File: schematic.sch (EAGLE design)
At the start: 65 parts, among them U1 ADP3338AKCZ-3.3RL7

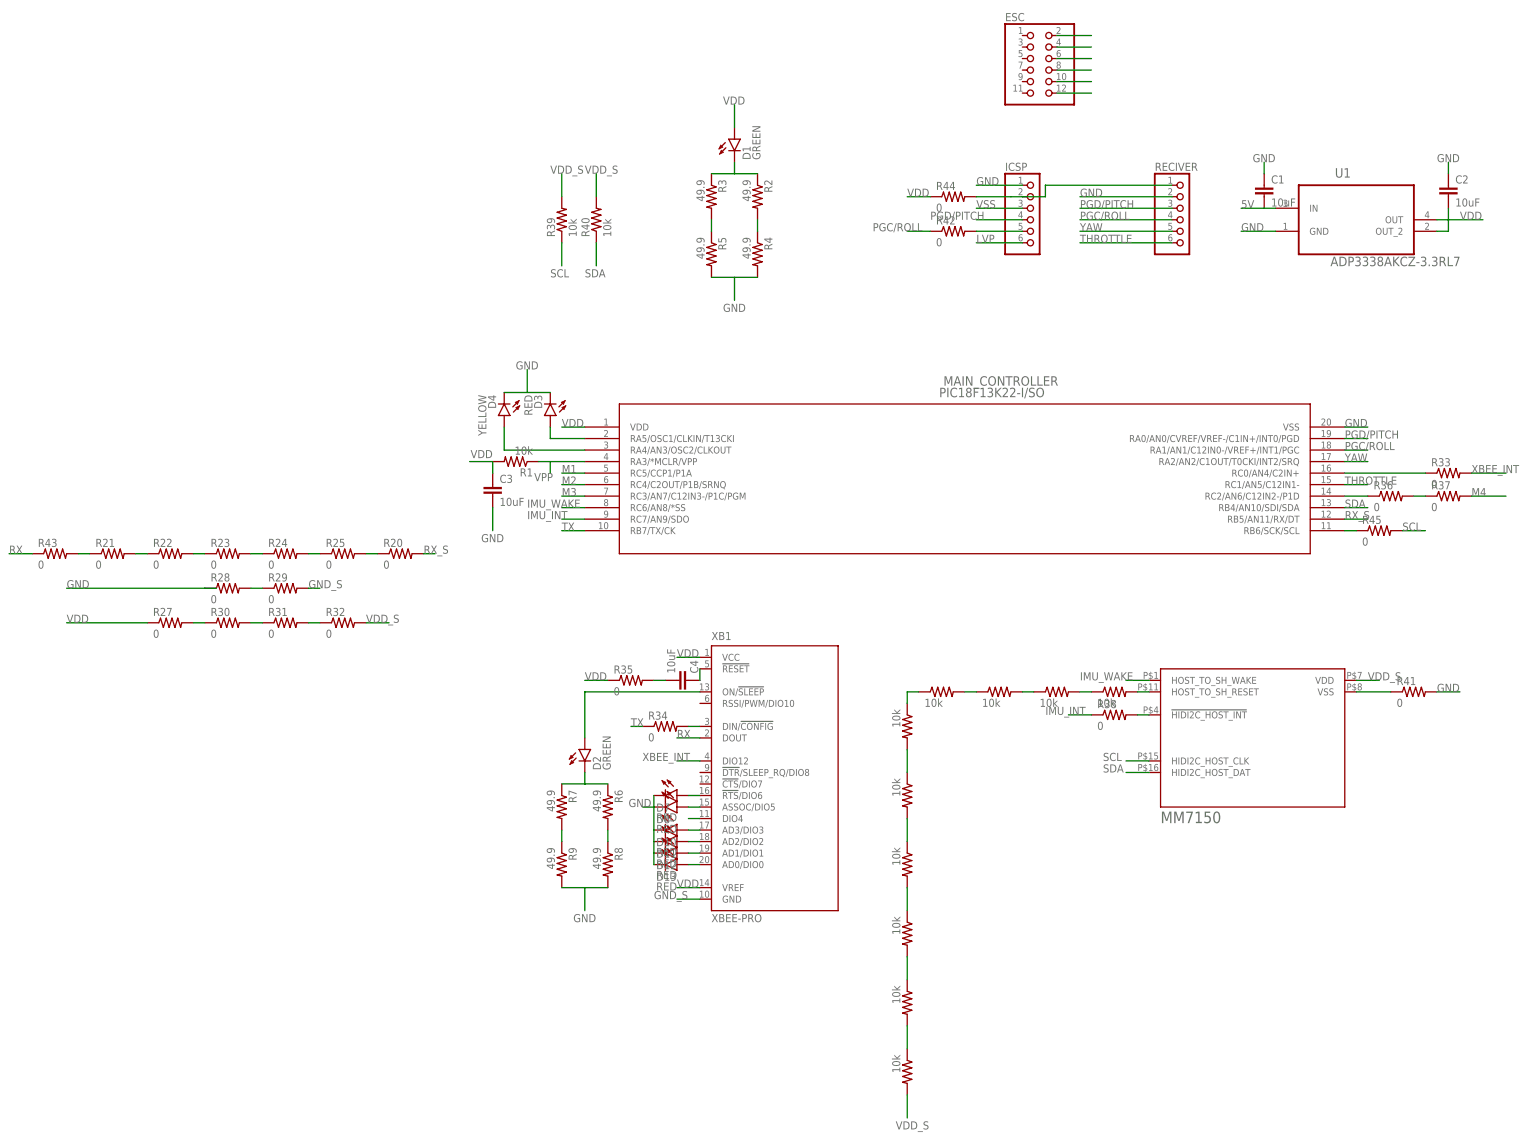
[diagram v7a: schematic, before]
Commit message: Removed jumper's from schematic and prepared for two layer board
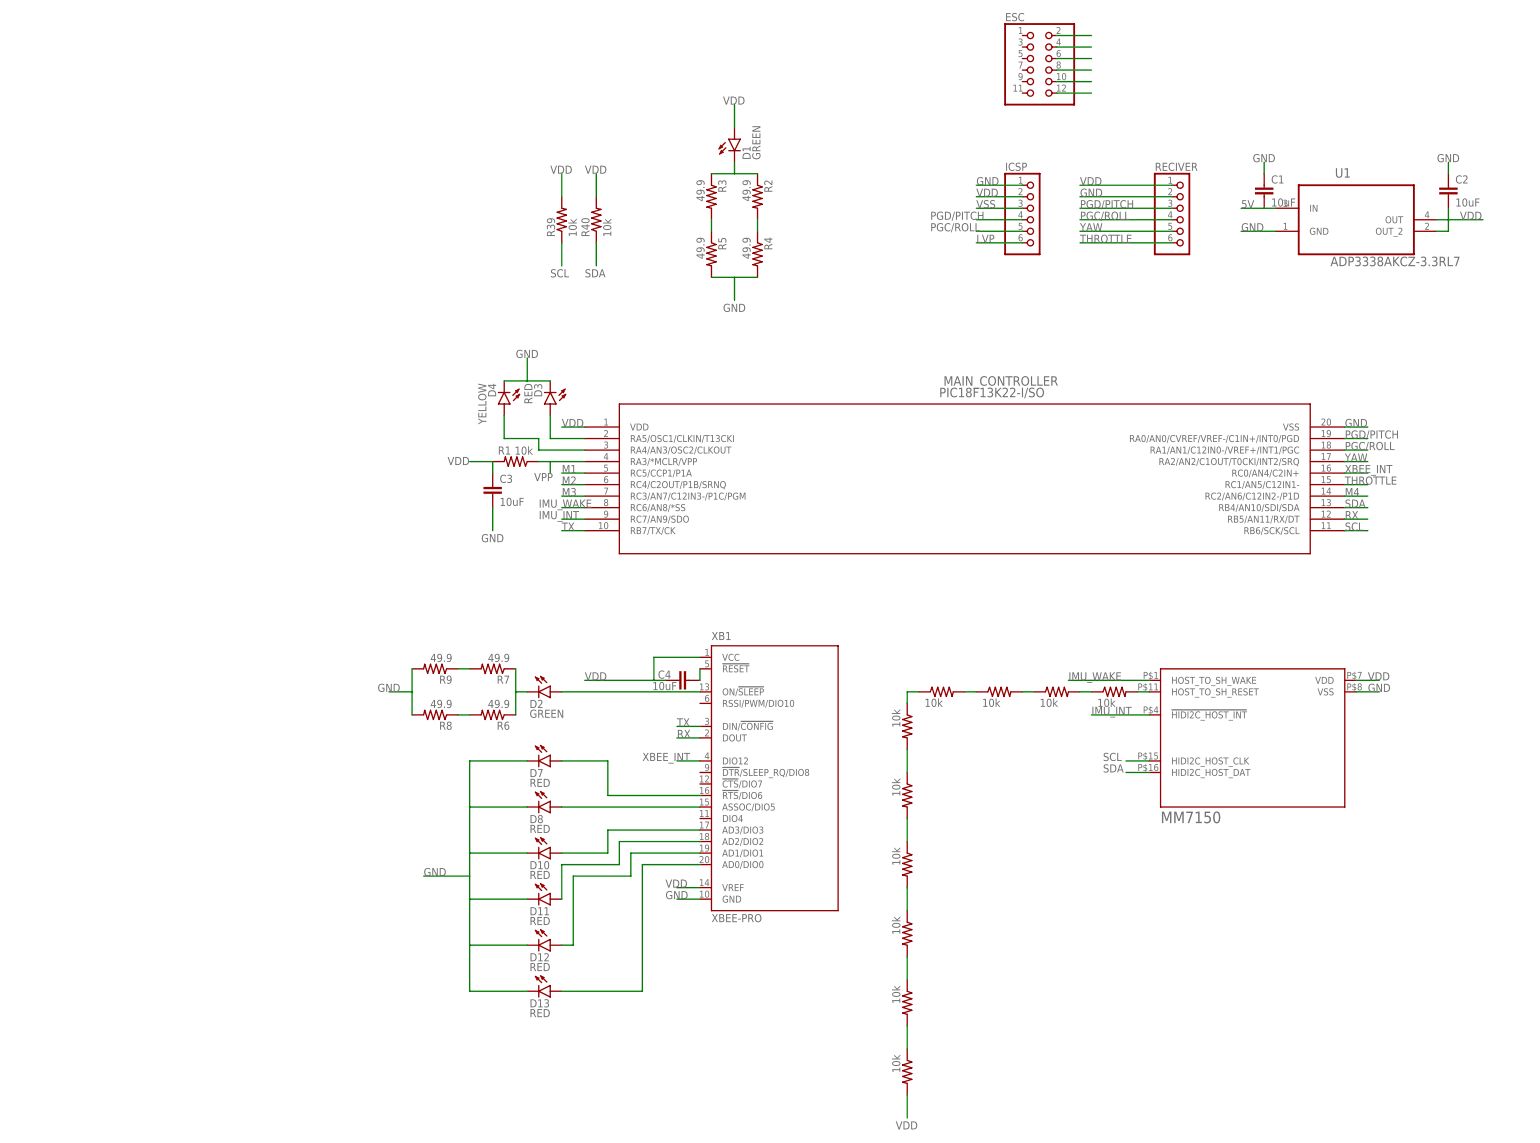
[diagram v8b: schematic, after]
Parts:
- removed R20, R21, R22, R23, R24, R25, R27, R28, R29, R30, R31, R32, R33, R34, R35, R36, R37, R38, R41, R42, R43, R44, R45: 0, SparkFun-Passives:RESISTOR0603-RES
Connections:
- removed net GND_S: R29.2, XB1.GND
- removed net N$1 (its old number): R20.1, R25.2
- removed net N$20 (its old number): R21.2, R22.1
- removed net N$21 (its old number): R22.2, R23.1
- removed net N$22 (its old number): R23.2, R24.1
- removed net N$23 (its old number): R24.2, R25.1
- removed net N$24: R28.2, R29.1
- removed net N$25: MAIN_CONTROLLER.RC0/AN4/C2IN+, R33.1
- removed net N$27: R27.2, R30.1
- removed net N$28: R30.2, R31.1
- removed net N$29: R31.2, R32.1
- removed net N$30: R34.2, XB1.DIN/!CONFIG
- removed net N$31: C4.2, R35.2
- removed net N$32: MAIN_CONTROLLER.RC2/AN6/C12IN2-/P1D, R36.1
- removed net N$33: R36.2, R37.1
- removed net N$34: IMU.!HIDI2C_HOST_INT, R38.2
- removed net N$35: IMU.VSS, R41.1
- removed net N$36: R21.1, R43.2
- removed net N$37: ICSP.5, R42.2
- removed net N$38: ICSP.2, R44.2, RECIVER.1
- removed net N$39: MAIN_CONTROLLER.RB6/SCK/SCL, R45.1
- removed net N$45: XB1.DIO4
- removed net RX_S: MAIN_CONTROLLER.RB5/AN11/RX/DT, R20.2
- removed net VDD_S: IMU.VDD, R19.2, R32.2, R39.2, R40.2
- net GND: now also IMU.VSS, XB1.GND; no longer R28.1, R41.2
- net IMU_INT: now also IMU.!HIDI2C_HOST_INT; no longer R38.1
- net M4: now also MAIN_CONTROLLER.RC2/AN6/C12IN2-/P1D; no longer R37.2
- net PGC/ROLL: now also ICSP.5; no longer R42.1
- net RX: now also MAIN_CONTROLLER.RB5/AN11/RX/DT; no longer R43.1
- net SCL: now also MAIN_CONTROLLER.RB6/SCK/SCL; no longer R45.2
- net TX: now also XB1.DIN/!CONFIG; no longer R34.1
- net VDD: now also C4.2, ICSP.2, IMU.VDD, R19.2, R39.2, R40.2, RECIVER.1; no longer R27.1, R35.1, R44.1
- net XBEE_INT: now also MAIN_CONTROLLER.RC0/AN4/C2IN+; no longer R33.2
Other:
- moved on the sheet: D10, D11, D12, D13, D2, D3, D4, D7, D8, R6, R7, R8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
